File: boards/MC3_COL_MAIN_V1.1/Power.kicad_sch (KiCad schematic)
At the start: 14 parts, among them J1 SUPPLY_IN, Q1 AO4407C, U1 AMS1117-3.3

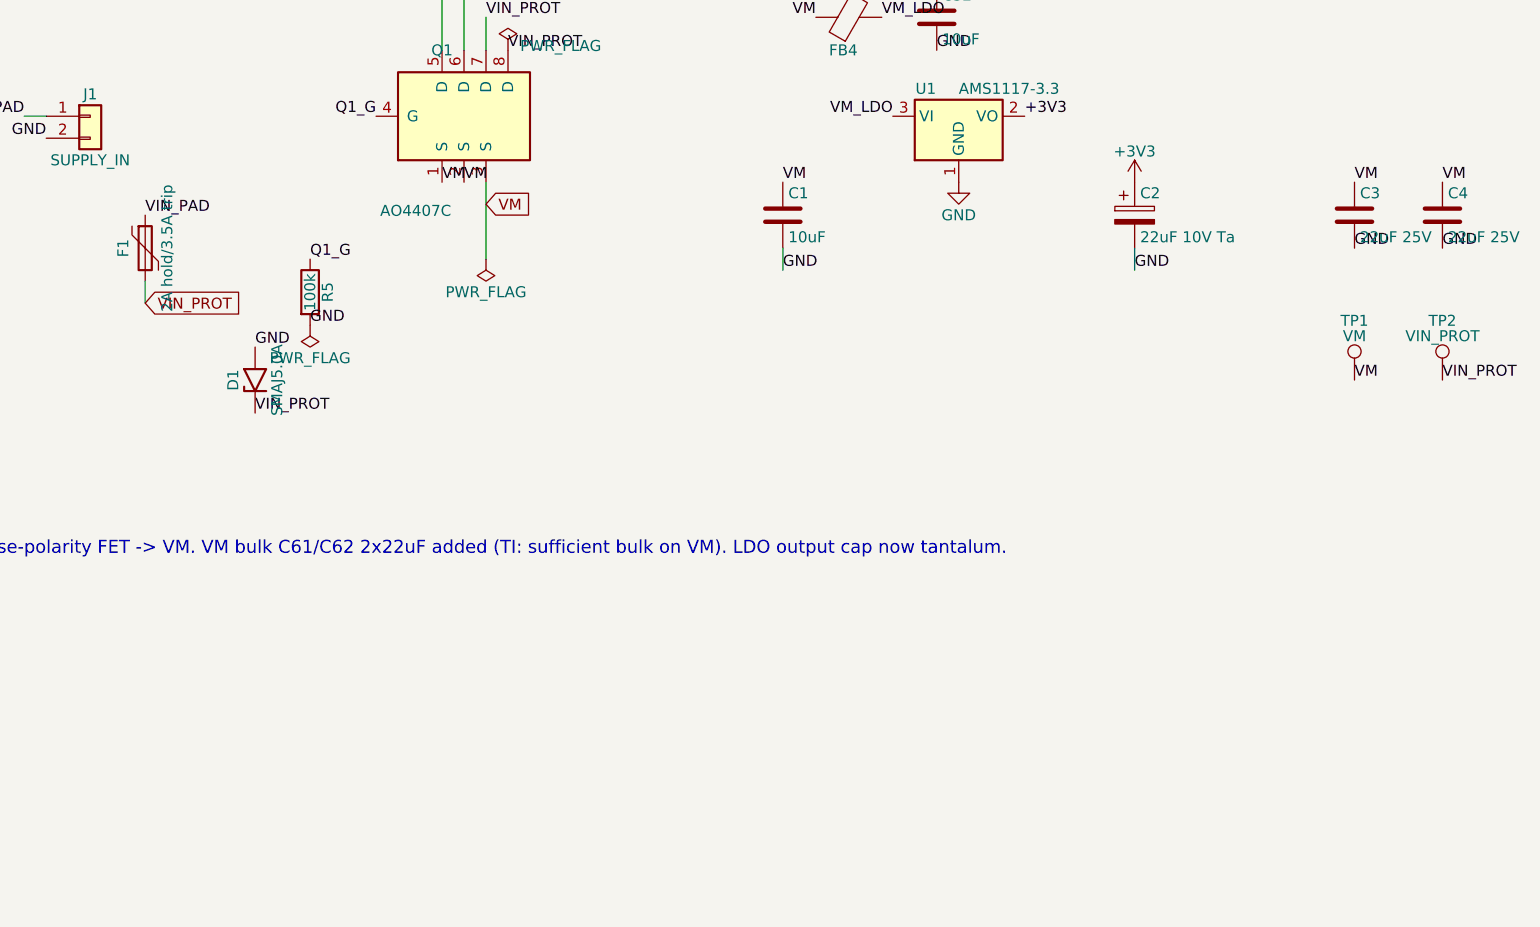
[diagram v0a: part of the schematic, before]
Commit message: V1.1: 24 V input - LM61460 sync buck (U12) + support, F1/D1/Q1 re-rated, D7 gate zener, BUCK_SYNC on PB4/LPTIM1_CH2, VIN24 netclass; ERC 0 errors
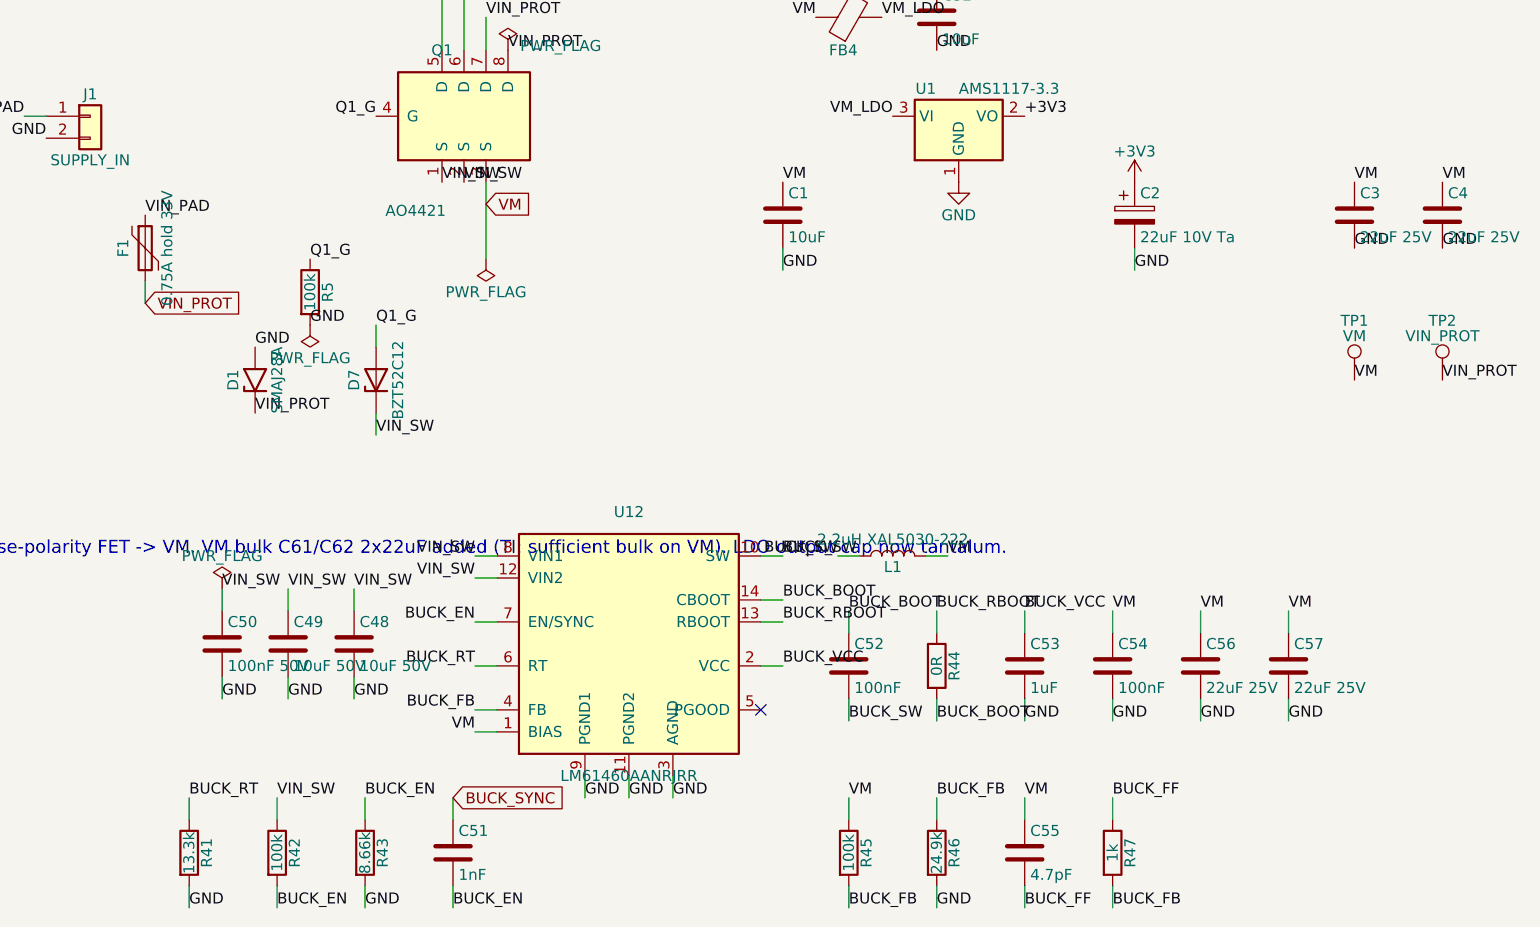
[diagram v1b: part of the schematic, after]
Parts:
- added C48, C49: 10uF 50V, MC3_COL_MAIN:C_1210_3225Metric, symbol Device:C
- added C50: 100nF 50V, MC3_COL_MAIN:C_0603_1608Metric, symbol Device:C
- added C51: 1nF, MC3_COL_MAIN:C_0402_1005Metric, symbol Device:C
- added C52, C54: 100nF, MC3_COL_MAIN:C_0402_1005Metric, symbol Device:C
- added C53: 1uF, MC3_COL_MAIN:C_0603_1608Metric, symbol Device:C
- added C55: 4.7pF, MC3_COL_MAIN:C_0402_1005Metric, symbol Device:C
- added C56, C57: 22uF 25V, MC3_COL_MAIN:C_0805_2012Metric, symbol Device:C
- added D7: BZT52C12, MC3_COL_MAIN:D_SOD-123, symbol Device:D_Zener
- added L1: 2.2uH XAL5030-222, MC3_COL_MAIN:L_Coilcraft_XAL5030-XXX, symbol Device:L
- added R41: 13.3k, MC3_COL_MAIN:R_0402_1005Metric, symbol Device:R
- added R42, R45: 100k, MC3_COL_MAIN:R_0402_1005Metric, symbol Device:R
- added R43: 8.66k, MC3_COL_MAIN:R_0402_1005Metric, symbol Device:R
- added R44: 0R, MC3_COL_MAIN:R_0402_1005Metric, symbol Device:R
- added R46: 24.9k, MC3_COL_MAIN:R_0402_1005Metric, symbol Device:R
- added R47: 1k, MC3_COL_MAIN:R_0402_1005Metric, symbol Device:R
- added U12: LM61460AANRJRR, MC3_COL_MAIN:VQFN-HR-14_RJR0014A, symbol MC3_COL_MAIN:LM61460
- D1: value SMAJ5.0A -> SMAJ28A; Note TVS SMAJ5.0A (unidirectional, 5 V standoff) VIN_PROT to GND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 -> 24 V input TVS: standoff 28 V, V_BR min 31.1 V, clamp 45.4 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
- F1: value 2A hold/3.5A trip -> 0.75A hold 33V; Note PROVISIONAL polyfuse 1206, ~2.5 A hold: board worst case 4.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 -> PROVISIONAL - 24 V input: at 24 V the board's power draws 1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
- Q1: value AO4407C -> AO4421; Note Reverse-polarity P-FET, drain to input, source to board; ga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 -> Reverse-polarity P-FET re-rated for 24 V: AO4421 -60 V / -6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
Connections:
- net GND: now also C48.2, C49.2, C50.2, C53.2, C54.2, C56.2, C57.2, R41.2, R43.2, R46.2, U12.11 (PGND2), U12.3 (AGND), U12.9 (PGND1)
- net Q1_G: now also D7.2 (A)
- net VM: now also C54.1, C55.1, C56.1, C57.1, L1.2, R45.1, U12.1 (BIAS); no longer Q1.1 (S), Q1.2 (S)
- new net BUCK_BOOT: C52.1, R44.2, U12.14 (CBOOT)
- new net BUCK_EN: C51.2, R42.2, R43.1, U12.7 (EN/SYNC)
- new net BUCK_FB: R45.2, R46.1, R47.2, U12.4 (FB)
- new net BUCK_FF: C55.2, R47.1
- new net BUCK_RBOOT: R44.1, U12.13 (RBOOT)
- new net BUCK_RT: R41.1, U12.6 (RT)
- new net BUCK_SW: C52.2, L1.1, U12.10 (SW)
- new net BUCK_SYNC: C51.1
- new net BUCK_VCC: C53.1, U12.2 (VCC)
- new net VIN_SW: C48.1, C49.1, C50.1, D7.1 (K), Q1.1 (S), Q1.2 (S), R42.1, U12.12 (VIN2), U12.8 (VIN1)
- no-connect marks 0 -> 1

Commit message: V1.1: MIGRATION s14 (24 V input delta), LM61460 layout note, CLAUDE.md current-boards
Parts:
- L1: Note Buck inductor per SNVSBD5D Table 9-2 (1 MHz / 5 V: 2.2 uH). Shielded, 5x5x3.1 mm - under the 4 mm cap; Isat ~9 A, 9.6 mOhm. Alternatives with the same land: XAL5030-332 (3.3 uH). Keep the SW-side pad short; nothing sensitive under it. -> Buck inductor per SNVSBD5D Table 9-2 (1 MHz / 5 V: 2.2 uH). Coilcraft XAL5030-222MEB: shielded molded, 5.48 x 5.28 x 3.1 mm (under the 4 mm cap), Isat 9.2 A, DCR 14.5 mOhm, 50 V rated. Same land: XAL5030-332 (3.3 uH). Keep the SW pad short; nothing sensitive under it.
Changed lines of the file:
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@@
 			)
 		)
-		(property "Note" "Buck inductor per SNVSBD5D Table 9-2 (1 MHz / 5 V: 2.2 uH). Shielded, 5x5x3.1 mm - under the 4 mm cap; Isat ~9 A, 9.6 mOhm. Alternatives with the same land: XAL5030-332 (3.3 uH). Keep the SW-side pad short; nothing sensitive under it."
+		(property "Note" "Buck inductor per SNVSBD5D Table 9-2 (1 MHz / 5 V: 2.2 uH). Coilcraft XAL5030-222MEB: shielded molded, 5.48 x 5.28 x 3.1 mm (under the 4 mm cap), Isat 9.2 A, DCR 14.5 mOhm, 50 V rated. Same land: XAL5030-332 (3.3 uH). Keep the SW pad short; nothing sensitive under it."
 			(at 132.08 130.81 0)
 			(hide yes)

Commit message: V1.1: U12 footprint = TI Ultra Librarian VQFN-HR14_RJR_TEX + RJR0014A STEP
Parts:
- U12: footprint MC3_COL_MAIN:VQFN-HR-14_RJR0014A -> MC3_COL_MAIN:VQFN-HR14_RJR_TEX
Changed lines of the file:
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@@
 			)
 		)
-		(property "Footprint" "MC3_COL_MAIN:VQFN-HR-14_RJR0014A"
+		(property "Footprint" "MC3_COL_MAIN:VQFN-HR14_RJR_TEX"
 			(at 101.6 140.97 0)
 			(hide yes)

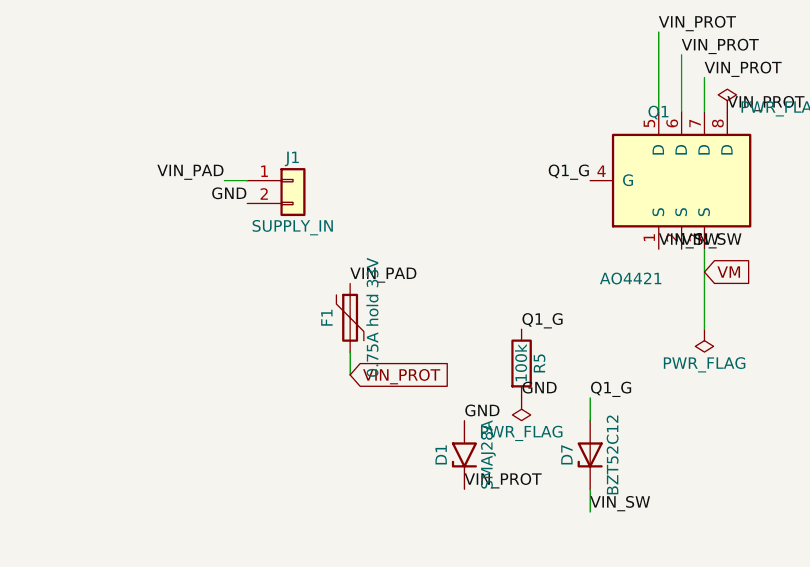
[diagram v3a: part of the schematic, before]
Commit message: V1.1: J13 machine-harness FFC (TE 84952-6, 1.0 mm 6-way) - YAW_OUT1/2 via new OUT1/OUT2 sheet pins, VIN_PAD/GND/CANH/CANL; ERC 0 errors
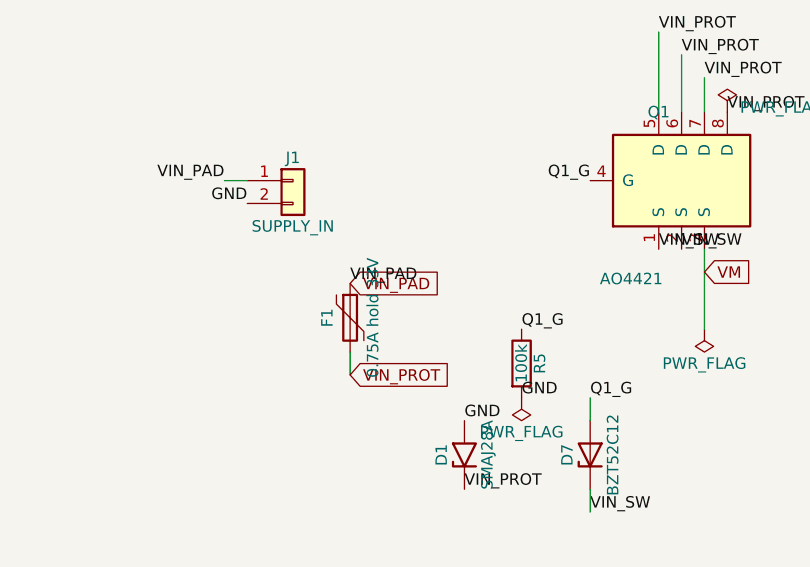
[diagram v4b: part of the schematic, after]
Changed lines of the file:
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@@
+		)
+	)
+	(global_label "VIN_PAD"
+		(shape input)
+		(at 45.72 91.44 0)
+		(effects
+			(font
+				(size 1.27 1.27)
+			)
+			(justify left)
 		)
 	)

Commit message: V1.1: F1 footprint -> 1812 (33 V polyfuse body)
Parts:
- F1: footprint MC3_COL_MAIN:Fuse_1206_3216Metric -> MC3_COL_MAIN:Fuse_1812_4532Metric
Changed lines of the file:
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@@
 			)
 		)
-		(property "Footprint" "MC3_COL_MAIN:Fuse_1206_3216Metric"
+		(property "Footprint" "MC3_COL_MAIN:Fuse_1812_4532Metric"
 			(at 45.72 95.25 0)
 			(hide yes)

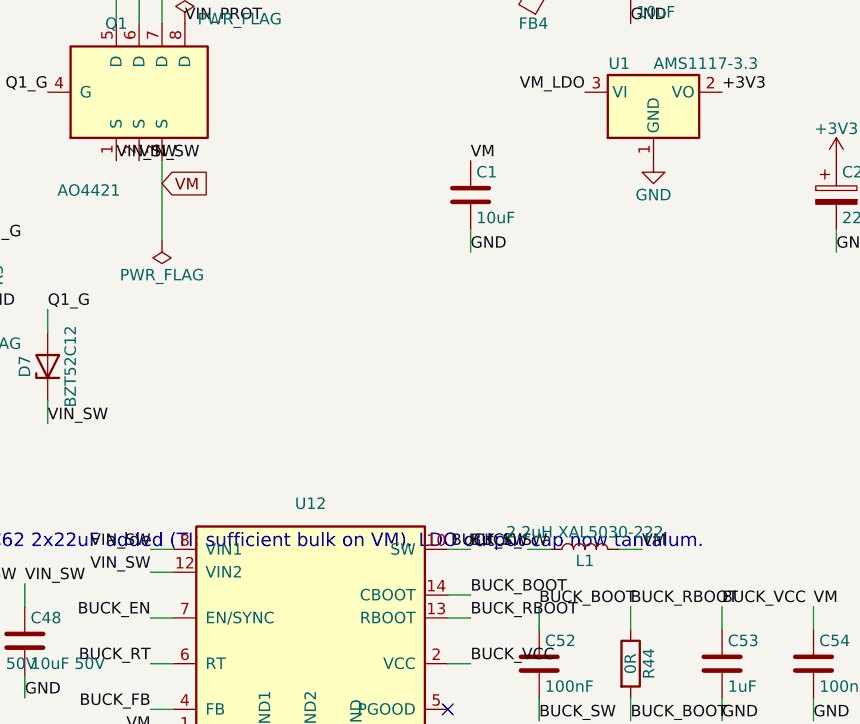
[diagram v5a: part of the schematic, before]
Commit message: V1.1: Q1 pin 3 onto VIN_SW (global VM label moved to the buck output); YAW_OUT netclass re-applied after KiCad close
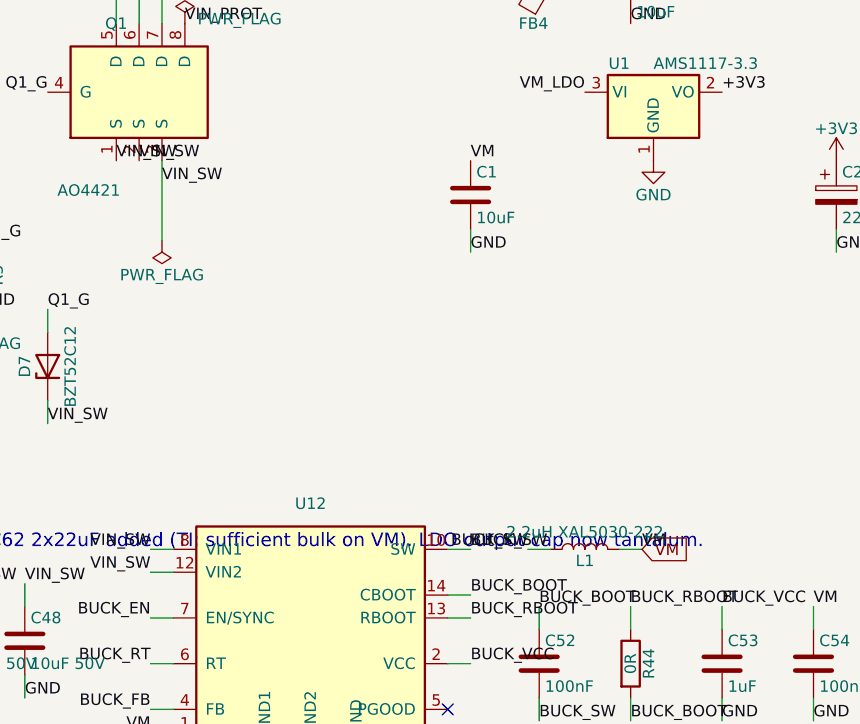
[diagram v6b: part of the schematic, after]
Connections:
- net VIN_SW: now also Q1.3 (S)
- net VM: no longer Q1.3 (S)
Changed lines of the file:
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@@
+		)
+	)
+	(label "VIN_SW"
+		(at 85.09 90.17 0)
+		(effects
+			(font
+				(size 1.27 1.27)
+			)
+			(justify left bottom)
 		)
 	)
@@
 		(property "Intersheetrefs" "${INTERSHEET_REFS}"
 			(at 45.72 101.6 0)
-			(hide yes)
-			(show_name no)
-			(do_not_autoplace no)
-			(effects
-				(font
-					(size 1.27 1.27)
-				)
-			)
-		)
-	)
-	(global_label "VM"
-		(shape input)
-		(at 85.09 90.17 0)
-		(effects
-			(font
-				(size 1.27 1.27)
-			)
-			(justify left)
-		)
-		(property "Intersheetrefs" "${INTERSHEET_REFS}"
-			(at 85.09 90.17 0)
 			(hide yes)
 			(show_name no)
@@
 		(effects
 			(font
+				(size 1.27 1.27)
+			)
+			(justify left)
+		)
+	)
+	(global_label "VM"
+		(shape input)
+		(at 138.43 130.81 0)
+		(effects
+			(font

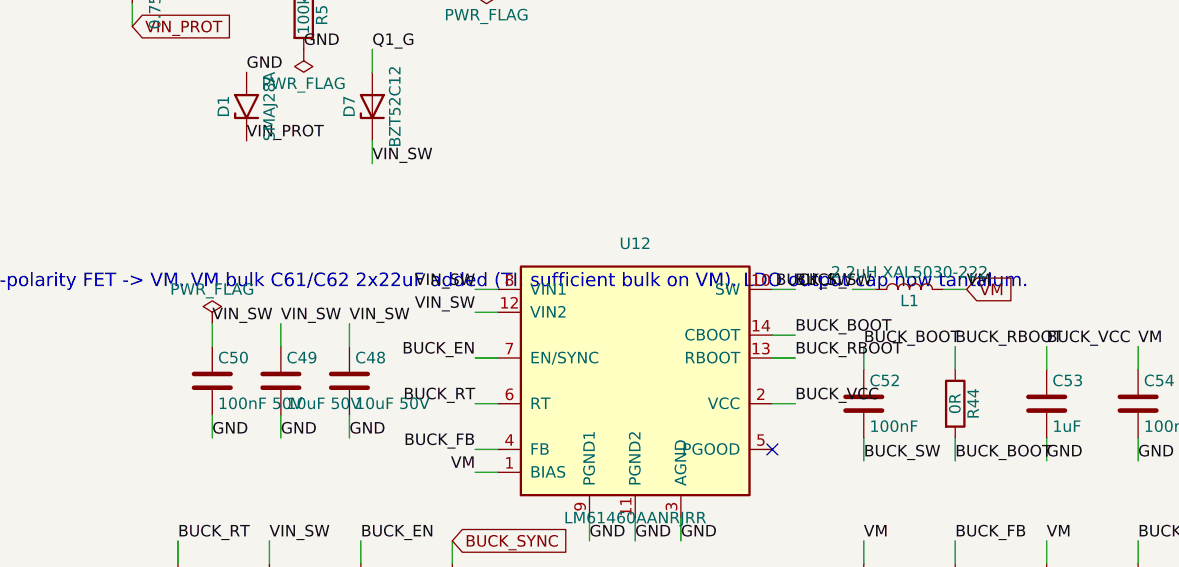
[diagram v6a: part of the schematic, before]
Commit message: V1.1: PWR_FLAG moved to VM at the buck output; ERC 0 errors
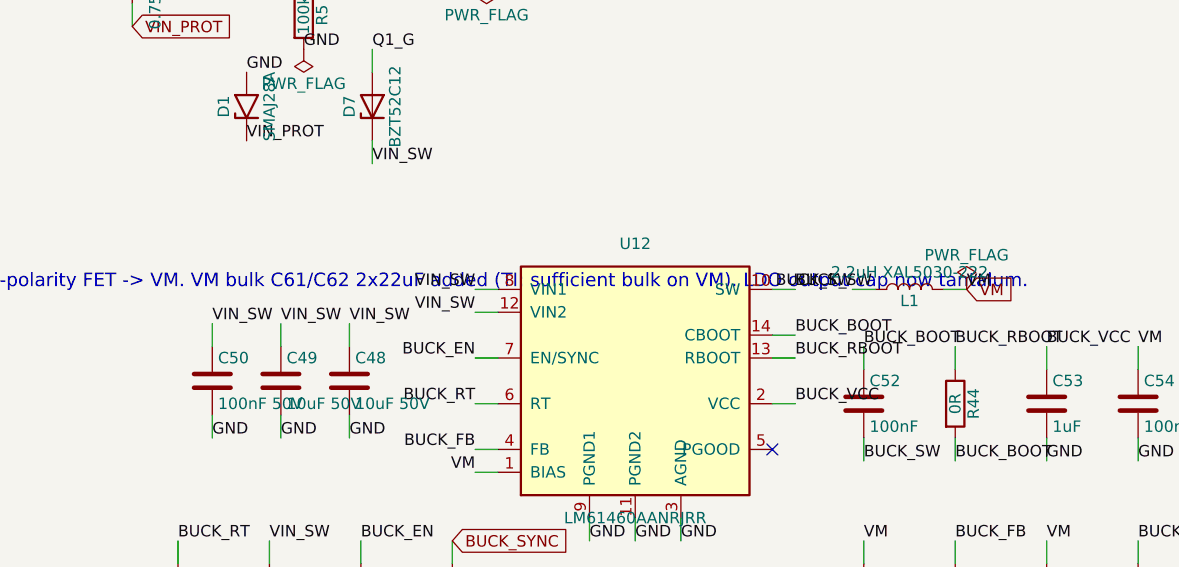
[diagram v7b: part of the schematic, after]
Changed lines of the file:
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@@
 	(symbol
 		(lib_id "power:PWR_FLAG")
-		(at 54.61 134.62 0)
+		(at 138.43 130.81 0)
 		(unit 1)
 		(in_bom yes)
 		(on_board yes)
 		(dnp no)
-		(property "Reference" "#PWR0127"
-			(at 54.61 132.715 0)
+		(property "Reference" "#PWR0128"
+			(at 138.43 128.905 0)
 			(hide yes)
 			(effects
@@
 		)
 		(property "Value" "PWR_FLAG"
-			(at 54.61 130.81 0)
+			(at 138.43 127 0)
 			(effects
 				(font
@@
 		)
 		(property "Footprint" ""
-			(at 54.61 134.62 0)
+			(at 138.43 130.81 0)
 			(hide yes)
 			(effects
@@
 		)
 		(property "Datasheet" ""
-			(at 54.61 134.62 0)
+			(at 138.43 130.81 0)
 			(hide yes)
 			(effects
@@
 			(project "Power"
 				(path "/62fa4f2c-604d-44f9-988f-2ce377285c9c"
-					(reference "#PWR0127")
+					(reference "#PWR0128")
 					(unit 1)
 				)

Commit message: V1.1 Power sheet: buck section redrawn as a wired left-to-right chain (netlist unchanged, ERC 0 errors)
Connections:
- net BUCK_FB: now also R47.1; no longer R47.2
- net BUCK_SYNC: now also C51.2; no longer C51.1
- net BUCK_BOOT: no longer names the net of C52.1, R44.2, U12.14 (CBOOT)
- net BUCK_EN: no longer names the net of R42.2, R43.1, U12.7 (EN/SYNC)
- net BUCK_EN: now also C51.1; no longer C51.2
- net BUCK_FF: no longer names the net of C55.2
- net BUCK_FF: now also R47.2; no longer R47.1
- net BUCK_RBOOT: no longer names the net of R44.1, U12.13 (RBOOT)
- net BUCK_RT: no longer names the net of R41.1, U12.6 (RT)
- net BUCK_VCC: no longer names the net of C53.1, U12.2 (VCC)
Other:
- moved on the sheet: C48, C49, C50, C51, C52, C53, C54, C55, C56, C57, L1, R41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
